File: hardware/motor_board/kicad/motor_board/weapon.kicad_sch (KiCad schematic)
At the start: 57 parts, among them Q1 HYG015N04LS1C2, Q2 HYG015N04LS1C2, Q3 HYG015N04LS1C2, Q4 HYG015N04LS1C2, Q5 HYG015N04LS1C2, Q6 HYG015N04LS1C2, U14 74LVC1G17SE-7, U2 DRV8323RHRGZR, U6 SN74LVC08APWR

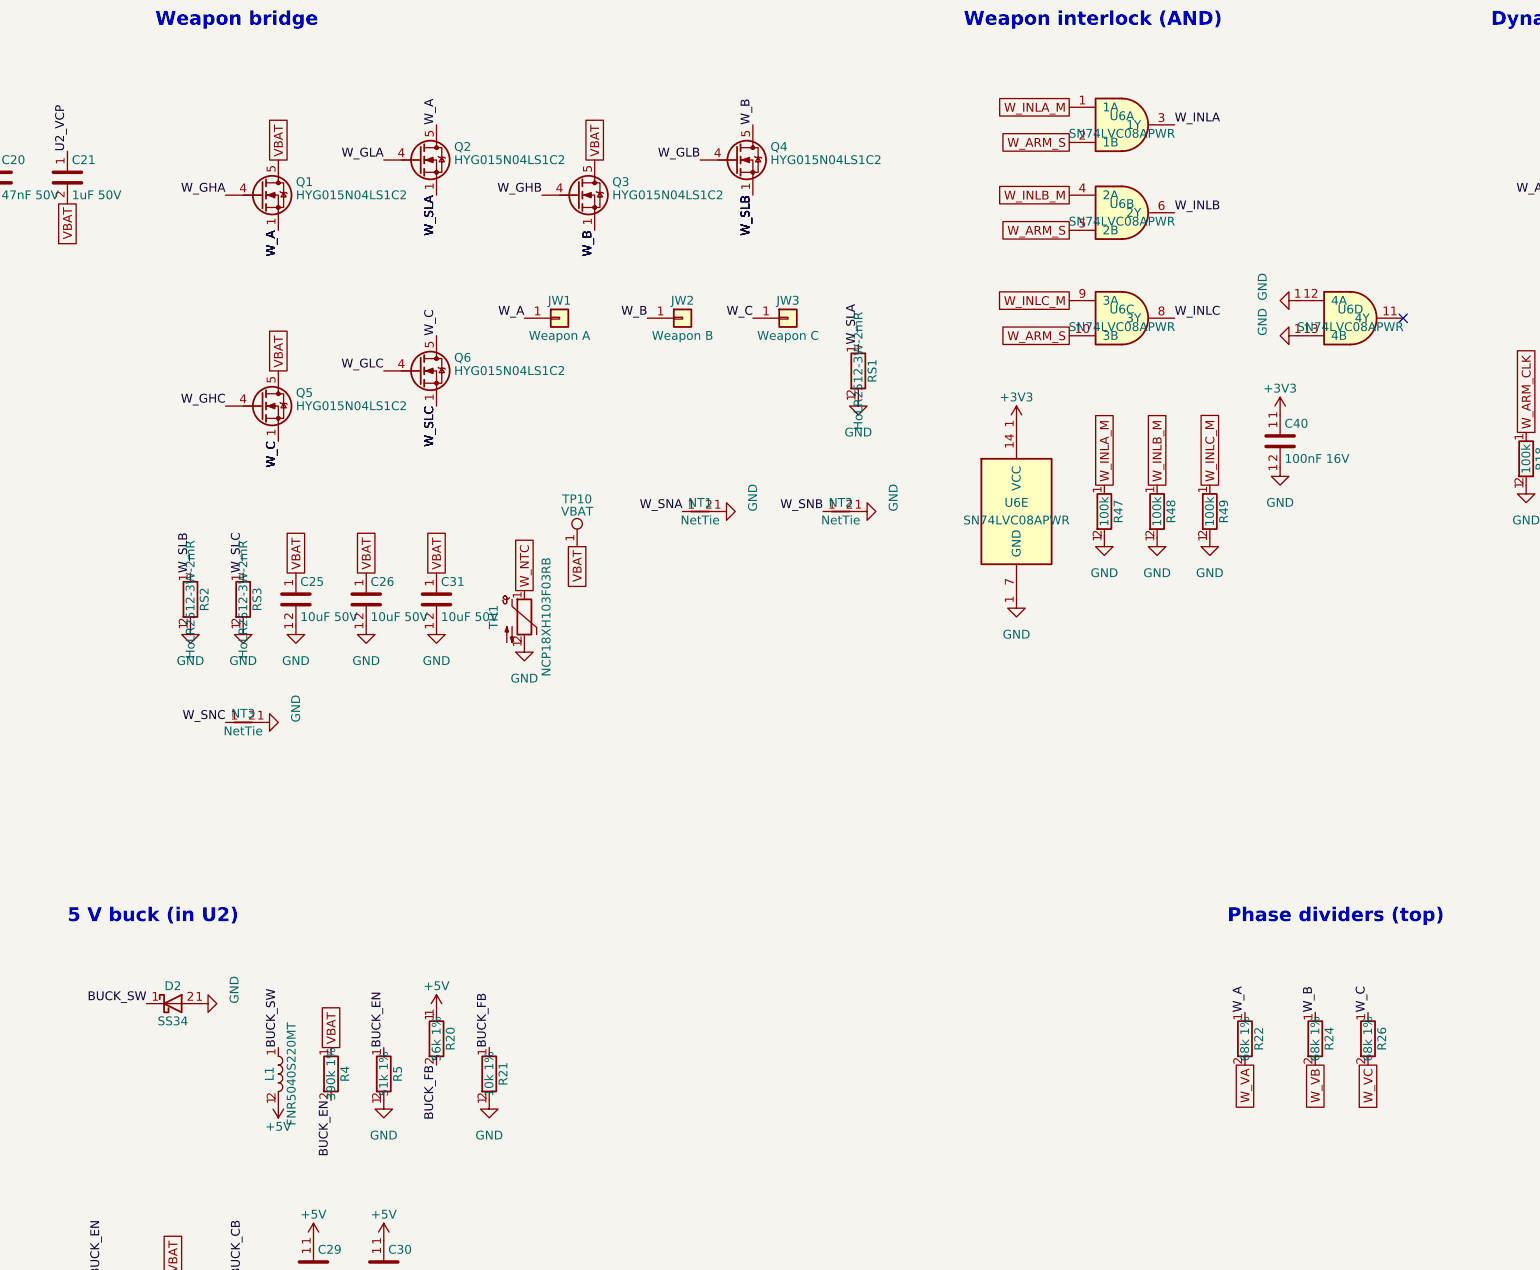
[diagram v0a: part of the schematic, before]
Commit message: v2 package swaps (rev L2), after adversarial review: U6 WQFN-14 (EP to GND), D2 PMEG4030ER, L1 ZEMS404030 4.1 mm, J4 vertical XH, J2/J3 genuine JST vertical SH, R300/R400 0603 anti-surge, R15/C14/D10 one size down; drive VM bulk 2 x 10 uF X7R 1210 per drive (C309/C310/C409/C410 removed, user OK) - the 1206 X5R kept only ~2.3 uF at 16.8 V
sim_hotplug.py models MLCC DC bias (worst bounce 2.14 V/us at 0 C, 2.62 at -40 C); library check 0 errors, mutation test all caught; schematic regenerated, nets 176/176; v2 board rebuilt: DRC 0, parity 0; WQFN-14 3D model generated; DESIGN/calcs/BOM/FAB/CHANGES updated (CPL rotation fix for J2/J3/J4)

Co-Authored-By: Claude Opus 5.5 (1M context) <noreply@anthropic.com>
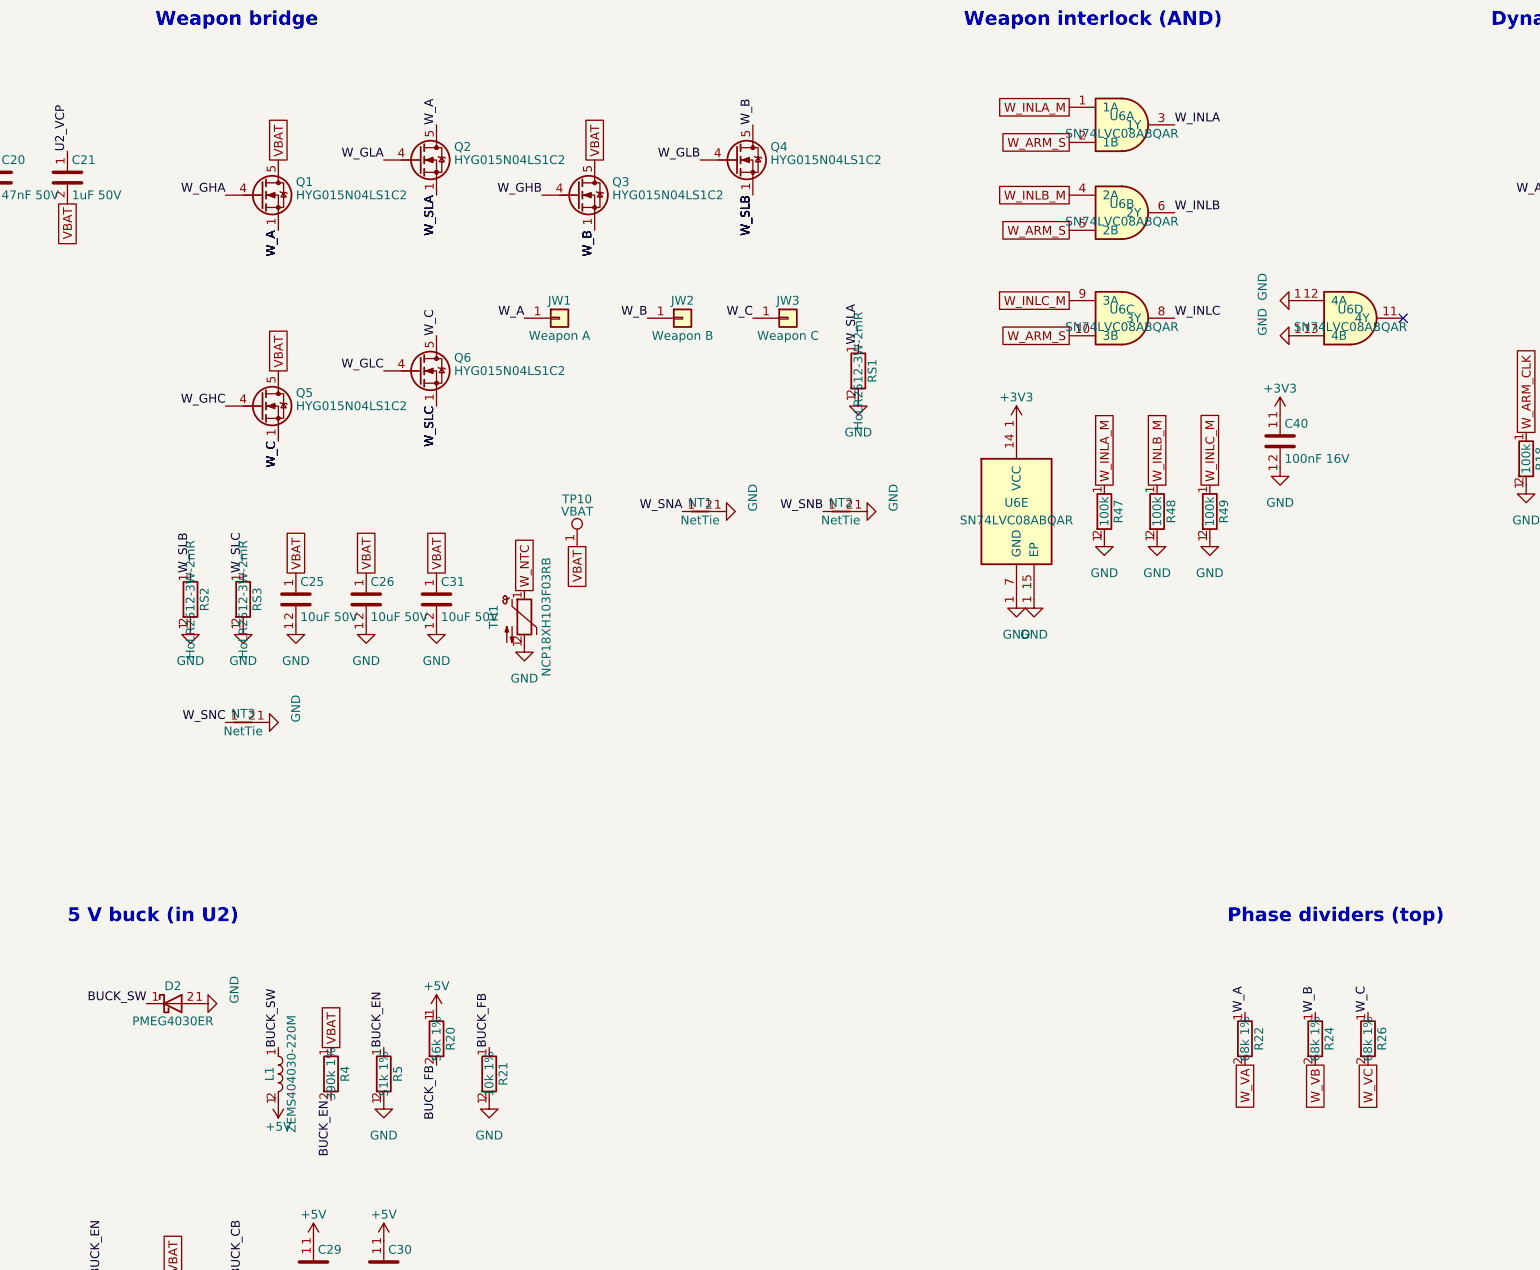
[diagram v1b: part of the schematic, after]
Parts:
- removed D2: SS34, Diode_SMD:D_SMA, symbol motor_board:SS34
- removed L1: FNR5040S220MT, Inductor_SMD:L_Changjiang_FNR5040S, symbol motor_board:FNR5040S220MT
- removed U6: SN74LVC08APWR, Package_SO:TSSOP-14_4.4x5mm_P0.65mm, symbol motor_board:SN74LVC08APWR
- added D2: PMEG4030ER, Diode_SMD:Nexperia_CFP3_SOD-123W, symbol motor_board:PMEG4030ER
- added L1: ZEMS404030-220M, Inductor_SMD:L_Changjiang_FTC404030S, symbol motor_board:ZEMS404030-220M
- added U6: SN74LVC08ABQAR, Package_DFN_QFN:DHWQFN-14-1EP_2.5x3mm_P0.5mm_EP1x1.5mm, symbol motor_board:SN74LVC08ABQAR
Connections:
- net +3V3: now also U6.14 (VCC)
- net +5V: now also L1.2
- net BUCK_SW: now also D2.1 (K), L1.1
- net GND: now also D2.2 (A), U6.12 (4A), U6.13 (4B), U6.15 (EP), U6.7 (GND)
- net W_ARM_S: now also U6.10 (3B), U6.2 (1B), U6.5 (2B)
- net W_INLA: now also U6.3 (1Y)
- net W_INLA_M: now also U6.1 (1A)
- net W_INLB: now also U6.6 (2Y)
- net W_INLB_M: now also U6.4 (2A)
- net W_INLC: now also U6.8 (3Y)
- net W_INLC_M: now also U6.9 (3A)

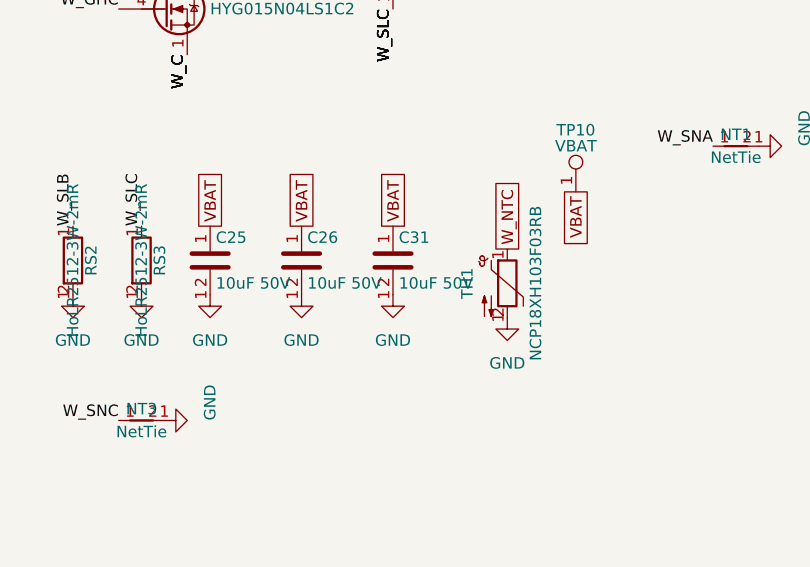
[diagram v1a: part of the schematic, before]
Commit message: C25/C26/C31 -> 10 uF 50 V X7R 1210 (C77102, user OK): VDS-only fault kick at the DRV8316 VM 7.7 -> 4.3 V/us, bus peak ~30 -> ~22 V; hot-plug worst 1.86 V/us (0 C), 2.14 (-40 C), re-close 1.77; schematic regenerated (nets 176/176), board rebuilt (DRC 0, parity 0); DESIGN/calcs/BOM/CHANGES updated
Co-Authored-By: Claude Opus 5.5 (1M context) <noreply@anthropic.com>
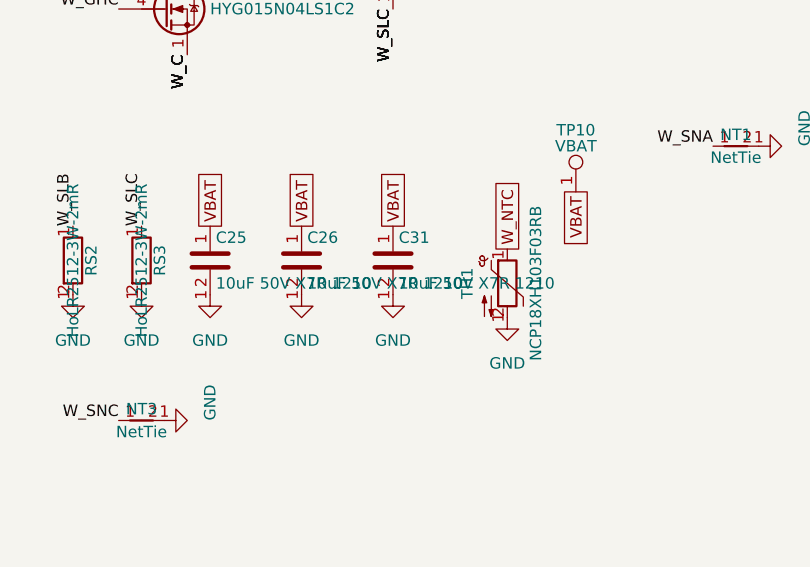
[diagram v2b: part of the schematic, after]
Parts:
- C25, C26, C31: value 10uF 50V -> 10uF 50V X7R 1210; footprint Capacitor_SMD:C_1206_3216Metric -> Capacitor_SMD:C_1210_3225Metric; LCSC C13585 -> C77102
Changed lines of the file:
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@@
 			)
 		)
-		(property "Value" "10uF 50V"
+		(property "Value" "10uF 50V X7R 1210"
 			(at 147.955 116.84 0)
 			(effects
@@
 			)
 		)
-		(property "Footprint" "Capacitor_SMD:C_1206_3216Metric"
+		(property "Footprint" "Capacitor_SMD:C_1210_3225Metric"
 			(at 148.2852 118.11 0)
 			(hide yes)
@@
 			)
 		)
-		(property "LCSC" "C13585"
+		(property "LCSC" "C77102"
 			(at 147.32 114.3 0)
 			(hide yes)
@@
 			)
 		)
-		(property "Value" "10uF 50V"
+		(property "Value" "10uF 50V X7R 1210"
 			(at 158.115 116.84 0)
 			(effects
@@
 			)
 		)
-		(property "Footprint" "Capacitor_SMD:C_1206_3216Metric"
+		(property "Footprint" "Capacitor_SMD:C_1210_3225Metric"
 			(at 158.4452 118.11 0)
 			(hide yes)
@@
 			)
 		)
-		(property "LCSC" "C13585"
+		(property "LCSC" "C77102"
 			(at 157.48 114.3 0)
 			(hide yes)
@@
 			)
 		)
-		(property "Value" "10uF 50V"
+		(property "Value" "10uF 50V X7R 1210"
 			(at 168.275 116.84 0)
 			(effects
@@
 			)
 		)
-		(property "Footprint" "Capacitor_SMD:C_1206_3216Metric"
+		(property "Footprint" "Capacitor_SMD:C_1210_3225Metric"
 			(at 168.6052 118.11 0)
 			(hide yes)
@@
 			)
 		)
-		(property "LCSC" "C13585"
+		(property "LCSC" "C77102"
 			(at 167.64 114.3 0)
 			(hide yes)
